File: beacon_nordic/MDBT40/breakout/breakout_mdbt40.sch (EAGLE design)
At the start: 12 parts

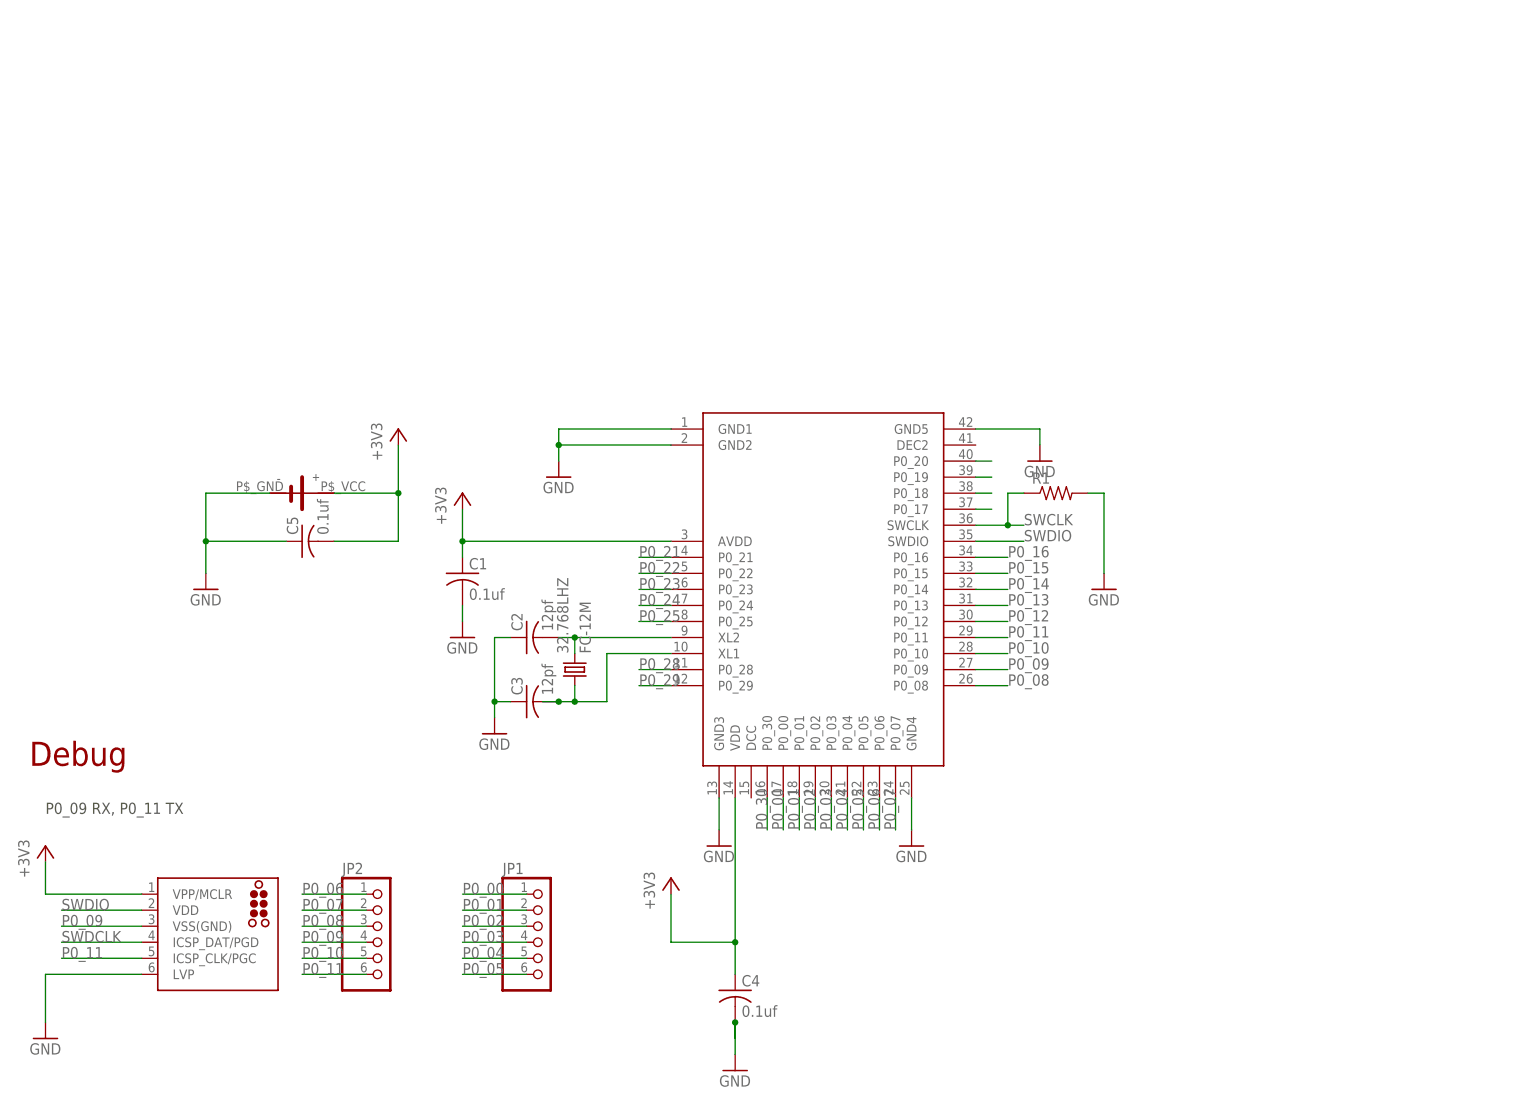
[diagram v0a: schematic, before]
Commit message: Update Breakout board
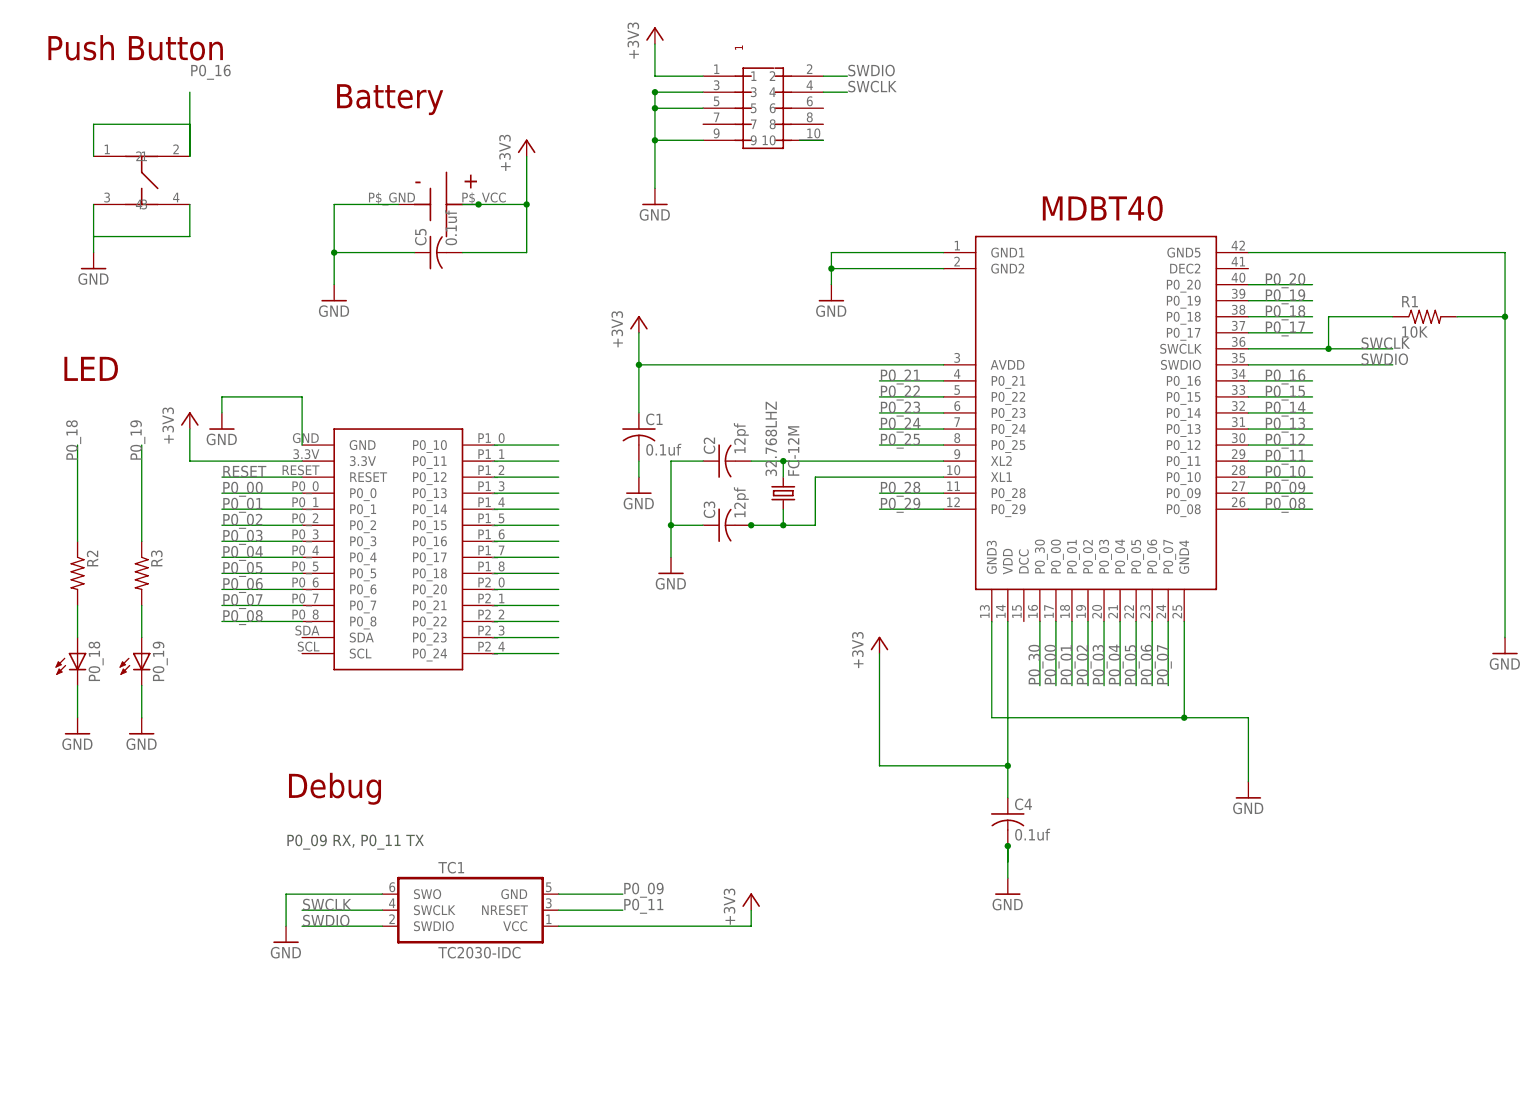
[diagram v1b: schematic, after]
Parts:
- removed J2: (no value), tag-connect:TC2030-MCP
- removed JP1, JP2: (no value), adafruit:PINHD-1X6
- added P0_18, P0_19: (no value), led:LEDCHIP-LED0603
- added R2, R3: (no value), adafruit:R-US_R0603
- added TC1: TC2030-IDC, TagConnect:TC2030-IDC
- added U$2: SMTU2450-TOP, GClue-Supply:SMTU2450-TOP
- added U$4: PIN-HEADER-SMT(1.27MM)2X5, gclue:PIN-HEADER-SMT(1.27MM)2X5
- added U$5: SWICTH-4P(KMR2), gclue-test:SWICTH-4P(KMR2)
- R1: value (none) -> 10K
- U$3: value SMTU2450-BOTTOM-MINI -> BREAKOUT_BLE_NORDIC; device gclue:SMTU2450-BOTTOM-MINI -> gclue:BREAKOUT_BLE_NORDIC
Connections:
- removed net N$21: U$1.P0_17
- removed net N$22: U$1.P0_18
- removed net N$23: U$1.P0_19
- removed net N$24: U$1.P0_20
- removed net SWDCLK: J2.ICSP_DAT/PGD
- new net N$1: P0_18.A, R2.2
- new net N$2: P0_19.A, R3.2
- new net P0_17: U$1.P0_17, U$3.P0_17
- new net P0_18: R2.1, U$1.P0_18, U$3.P0_18
- new net P0_19: R3.1, U$1.P0_19
- new net P0_20: U$1.P0_20, U$3.P0_20
- new net RESET: U$3.RESET
- new net RESET1: U$4.10
- net +3V3: now also TC1.VCC, U$2.+, U$3.3.3V, U$4.1; no longer J2.VPP/MCLR, U$3.P$_VCC
- net GND: now also P0_18.C, P0_19.C, TC1.SWO, U$2.-, U$3.GND, U$4.3, U$4.5, U$4.9, U$5.3, U$5.4; no longer J2.LVP, U$3.P$_GND
- net P0_00: now also U$3.P0_0; no longer JP1.1
- net P0_01: now also U$3.P0_1; no longer JP1.2
- net P0_02: now also U$3.P0_2; no longer JP1.3
- net P0_03: now also U$3.P0_3; no longer JP1.4
- net P0_04: now also U$3.P0_4; no longer JP1.5
- net P0_05: now also U$3.P0_5; no longer JP1.6
- net P0_06: now also U$3.P0_6; no longer JP2.1
- net P0_07: now also U$3.P0_7; no longer JP2.2
- net P0_08: now also U$3.P0_8; no longer JP2.3
- net P0_09: now also TC1.GND; no longer J2.VSS(GND), JP2.4
- net P0_10: now also U$3.P0_10; no longer JP2.5
- net P0_11: now also TC1.NRESET, U$3.P0_11; no longer J2.ICSP_CLK/PGC, JP2.6
- net P0_12: now also U$3.P0_12
- net P0_13: now also U$3.P0_13
- net P0_14: now also U$3.P0_14
- net P0_15: now also U$3.P0_15
- net P0_16: now also U$3.P0_16, U$5.1, U$5.2
- net P0_21: now also U$3.P0_21
- net P0_22: now also U$3.P0_22
- net P0_23: now also U$3.P0_23
- net P0_24: now also U$3.P0_24
- net SWCLK: now also TC1.SWCLK, U$4.4
- net SWDIO: now also TC1.SWDIO, U$4.2; no longer J2.VDD
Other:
- note added: "Battery"
- note added: "LED"
- note added: "MDBT40"
- note added: "Push Button"
- moved on the sheet: 32.768LHZ, C1, C2, C3, C4, C5, R1
